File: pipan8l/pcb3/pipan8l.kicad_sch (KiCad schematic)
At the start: 56 parts, among them J1 2x18edgecon, J2 2x18edgecon, J3 2x18edgecon, J4 2x18edgecon, J5 Conn_02x20_Odd_Even, J6 Conn_01x02_Pin, J7 Conn_01x16, J8 Conn_01x12, Q1 2N3906, Q10 2N3906, Q11 2N3906, Q12 2N3906, Q13 2N3906, Q14 2N3906, Q15 2N3906, Q16 2N3906, Q2 2N3906, Q3 2N3906, Q4 2N3906, Q5 2N3906, Q6 2N3906, Q7 2N3906, Q8 2N3906, Q9 2N3906, U1 MCP23017, U2 MCP23017, U3 MCP23017, U4 MCP23017

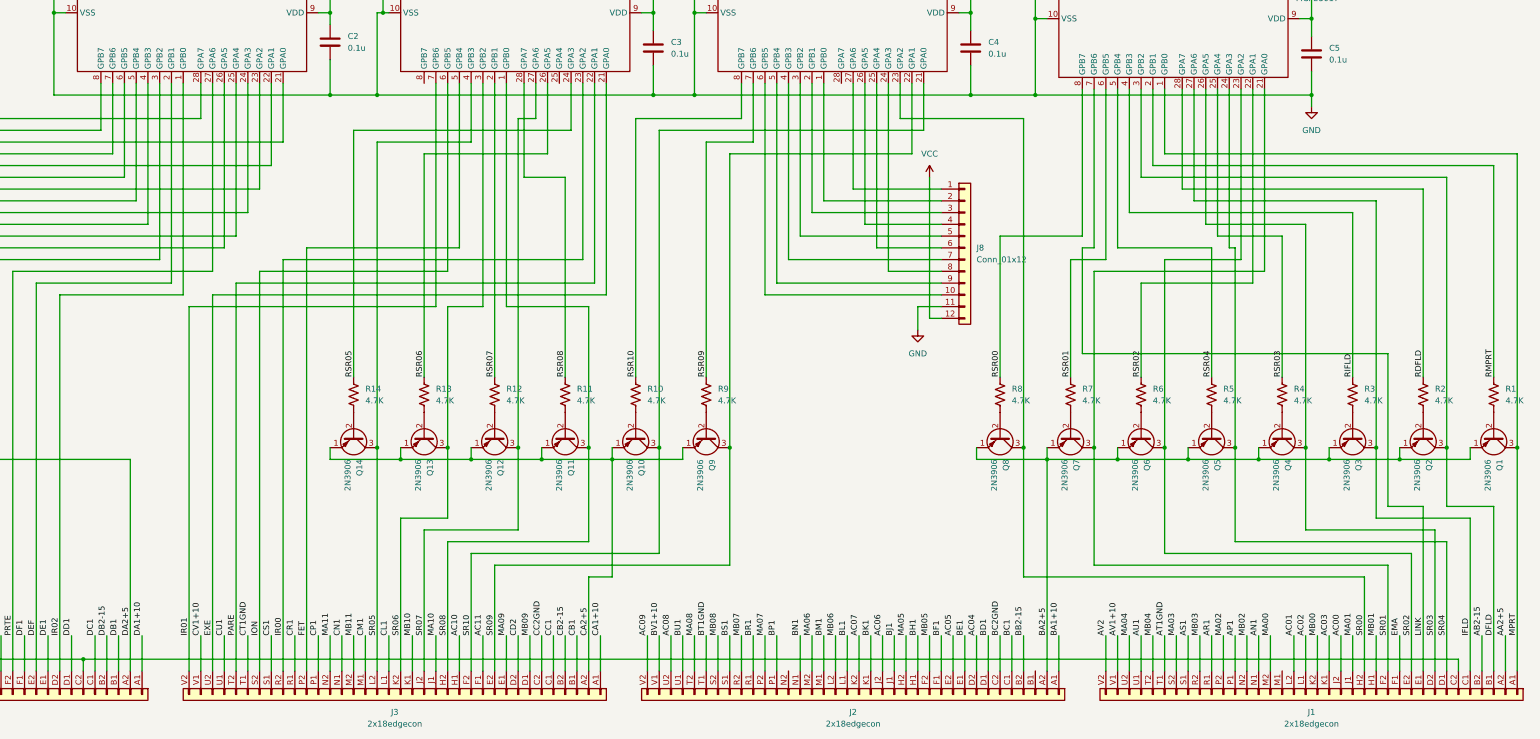
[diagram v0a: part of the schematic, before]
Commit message: add pipan8l/pcb3x and little updates for pcb3
  pcb3  - plugs into backplane for console access with console in place
  pcb3x - backplane pin straightener/insulator/spacer for use with pcb3
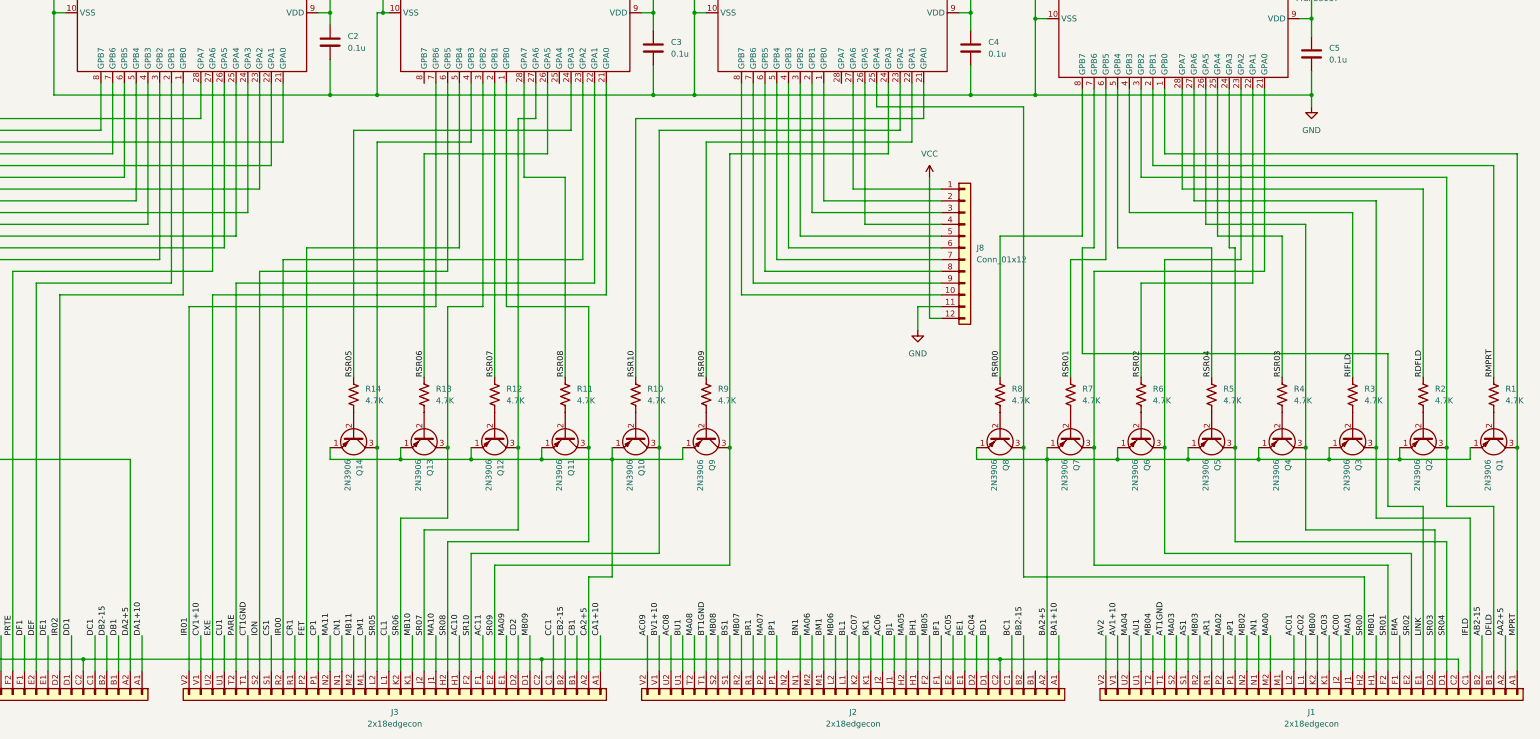
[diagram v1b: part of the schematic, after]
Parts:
- J1: footprint mypipan8lfoots:backpins -> mypipan8lfoots:backpins-A
- J2: footprint mypipan8lfoots:backpins -> mypipan8lfoots:backpins-B
- J3: footprint mypipan8lfoots:backpins -> mypipan8lfoots:backpins-C
- J4: footprint mypipan8lfoots:backpins -> mypipan8lfoots:backpins-D
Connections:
- net BC2GND is gone; now on net GND: J2.C2
- net CC2GND is gone; now on net GND: J3.C2
- net RSR09: now also U2.22 (GPA1); no longer U2.7 (GPB6)
- net RSR10: now also U2.21 (GPA0); no longer U2.8 (GPB7)
- net SR00: now also U2.25 (GPA4); no longer U2.23 (GPA2)
- net SR09: now also U2.24 (GPA3); no longer U2.22 (GPA1)
- net SR10: now also U2.23 (GPA2); no longer U2.21 (GPA0)
- net at J8.8 (Pin_8): now also U2.6 (GPB5); no longer U2.24 (GPA3)
- net at J8.6 (Pin_6): now also U2.4 (GPB3); no longer U2.25 (GPA4)
- net at J8.7 (Pin_7): now also U2.5 (GPB4); no longer U2.4 (GPB3)
- net at J8.9 (Pin_9): now also U2.7 (GPB6); no longer U2.5 (GPB4)
- net at J8.10 (Pin_10): now also U2.8 (GPB7); no longer U2.6 (GPB5)
